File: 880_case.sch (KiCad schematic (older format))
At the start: 169 parts, among them CON1 BARREL_JACK, J1 RUN/STOP, J10 RS IN, J11 CP IN, J12 MA IN, J13 CB IN, J14 CY IN, J15 OH IN, J16 CH IN, J17 IN 1, J18 IN 2, J19 IN 3, J2 SYNC24 CLK, J20 IN 4, J21 MULT IN, J22 SUM, J23 JACK_STEREO, J24 JACK_TRS_SWITCHED, J3 ASSIGN 1, J4 ASSIGN 2, J5 BD IN, J6 SD IN, J7 LT IN, J8 MT IN, J9 HT IN, P1 CONN_02X03, P2 CONN_01X02, P3 CONN_02X08, P4 CONN_01X03, P5 CONN_01X04, P6 CONN_01X04, P7 CONN_01X03, P8 CONN_01X03, P9 CONN_01X03, Q1 MMBT3904, Q10 MMBT3904, Q11 MMBT3904, Q12 MMBT3904, Q13 MMBT3904, Q14 C945, Q15 A733, Q2 MMBT3904, Q3 MMBT3904, Q4 MMBT3904, Q5 MMBT3904, Q6 MMBT3904, Q7 MMBT3904, Q8 MMBT3904, Q9 MMBT3904, U1 74HC165, U2 74HC165, U3 VX078-500, U4 VX078-500, U5 4558, U6 4558, X1 MIDI OUT, X2 SYNC24

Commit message: more edits
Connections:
- net at J24.1 (S): now also P6.1 (P1)
- net at J24.2 (T): now also P6.2 (P2)
- net at J24.3 (TB): now also J24.5 (R), P6.3 (P3)
- net at J24.4 (RB): now also P6.4 (P4)
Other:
- note added: "R"
- note added: "RB"
- note added: "S"
- note added: "T"
- moved on the sheet: J24
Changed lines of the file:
@@
 	15200 3750 15875 3750
-$Comp
-L JACK_TRS_SWITCHED J24
-U 1 1 5C60F07A
-P 16500 1475
-F 0 "J24" H 15950 1375 60  0000 C CNN
-F 1 "JACK_TRS_SWITCHED" H 16425 1725 60  0000 C CNN
-F 2 "MyModules:RA49B14B_SWITCHCRAFT" H 16400 1475 60  0001 C CNN
-F 3 "" H 16400 1475 60  0000 C CNN
-	1    16500 1475
-	-1   0    0    -1
-$EndComp
 $Comp
 L CONN_01X03 P8
@@
 Wire Wire Line
 	21500 3875 21250 3875
-Wire Wire Line
-	16250 1325 15925 1325
-Wire Wire Line
-	16250 1425 15925 1425
-Wire Wire Line
-	15925 1600 16250 1600
 $Comp
 L R_US R67
@@
 $EndComp
 Wire Wire Line
-	15925 1500 16250 1500
-Wire Wire Line
-	15925 1500 15925 1525
-Wire Wire Line
-	15925 1600 15925 1625
-Wire Wire Line
 	15325 1625 15050 1625
 Wire Wire Line
@@
 	15050 2000 14925 2000
 Connection ~ 14925 2000
-Wire Wire Line
-	16250 1675 16100 1675
-Wire Wire Line
-	16100 1675 16100 1500
-Connection ~ 16100 1500
 $Comp
 L CONN_01X04 P5
@@
 NoConn ~ 20875 12275
 NoConn ~ 20875 12375
+Text Notes 15275 1325 0    50   ~ 0
+S
+Text Notes 15275 1525 0    50   ~ 0
+R
+$Comp
+L JACK_TRS_SWITCHED J24
+U 1 1 5C60F07A
+P 16525 1500
+F 0 "J24" H 15975 1400 60  0000 C CNN
+F 1 "JACK_TRS_SWITCHED" H 16450 1750 60  0000 C CNN
+F 2 "MyModules:RA49B14B_SWITCHCRAFT" H 16425 1500 60  0001 C CNN
+F 3 "" H 16425 1500 60  0000 C CNN
+	1    16525 1500
+	-1   0    0    1
+$EndComp
+Wire Wire Line
+	15925 1325 16150 1325
+Text Notes 15275 1625 0    50   ~ 0
+RB
+Text Notes 15275 1425 0    50   ~ 0
+T
+Wire Wire Line
+	16150 1425 16050 1425
+Wire Wire Line
+	16050 1425 16050 1675
+Wire Wire Line
+	16050 1675 16150 1675
+Wire Wire Line
+	15925 1525 16050 1525
+Connection ~ 16050 1525
+Wire Wire Line
+	16150 1500 16125 1500
+Wire Wire Line
+	16125 1500 16125 1450
+Wire Wire Line
+	16125 1450 15925 1450
+Wire Wire Line
+	15925 1450 15925 1425
+Wire Wire Line
+	16150 1600 15925 1600
+Wire Wire Line
+	15925 1600 15925 1625
 $EndSCHEMATC

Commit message: added power switch and balanced jack sub boards
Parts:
- added J25: JACK_STEREO, MyModules:11XPC-SWITCH_CRAFT, symbol JACK_STEREO
- added P10: CONN_01X02, Pin_Headers:Pin_Header_Straight_1x02_Pitch2.54mm, symbol CONN_01X02
- added P11: CONN_01X03, Pin_Headers:Pin_Header_Straight_1x03_Pitch2.54mm, symbol CONN_01X03
- added SW1: SPST, MyModules:PR_PPR_ROCKER_SW, symbol SPST
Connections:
- new net: P10.1 (P1), SW1.2
- new net: P10.2 (P2), SW1.1
- new net: J25.1, P11.1 (P1)
- new net: J25.2, P11.2 (P2)
- new net: J25.3, P11.3 (P3)
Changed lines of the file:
@@
 Wire Wire Line
 	12125 4125 12125 4300
-Text Notes 19225 2475 0    100  ~ 0
+Text Notes 19125 2075 0    100  ~ 0
 TO TRS OUT
 $Comp
@@
 Wire Wire Line
 	15925 1600 15925 1625
+$Comp
+L CONN_01X02 P10
+U 1 1 5CF5764A
+P 14875 11125
+F 0 "P10" H 14875 11275 50  0000 C CNN
+F 1 "CONN_01X02" V 14975 11125 50  0000 C CNN
+F 2 "Pin_Headers:Pin_Header_Straight_1x02_Pitch2.54mm" H 14875 11125 60  0001 C CNN
+F 3 "" H 14875 11125 60  0000 C CNN
+	1    14875 11125
+	0    1    1    0
+$EndComp
+$Comp
+L SPST SW1
+U 1 1 5CF577D2
+P 14825 10375
+F 0 "SW1" H 14825 10475 50  0000 C CNN
+F 1 "SPST" H 14825 10275 50  0000 C CNN
+F 2 "MyModules:PR_PPR_ROCKER_SW" H 14825 10375 60  0000 C CNN
+F 3 "" H 14825 10375 60  0000 C CNN
+	1    14825 10375
+	1    0    0    -1
+$EndComp
+Wire Wire Line
+	14325 10375 14325 10925
+Wire Wire Line
+	15325 10375 15325 10925
+Wire Wire Line
+	14325 10925 14825 10925
+Wire Wire Line
+	15325 10925 14925 10925
+$Comp
+L JACK_STEREO J25
+U 1 1 5CF60EBD
+P 19950 2475
+F 0 "J25" H 19400 2375 60  0000 C CNN
+F 1 "JACK_STEREO" H 19700 2675 60  0000 C CNN
+F 2 "MyModules:11XPC-SWITCH_CRAFT" H 19850 2475 60  0001 C CNN
+F 3 "" H 19850 2475 60  0000 C CNN
+	1    19950 2475
+	-1   0    0    -1
+$EndComp
+$Comp
+L CONN_01X03 P11
+U 1 1 5CF61677
+P 19350 2425
+F 0 "P11" H 19350 2625 50  0000 C CNN
+F 1 "CONN_01X03" V 19450 2425 50  0000 C CNN
+F 2 "Pin_Headers:Pin_Header_Straight_1x03_Pitch2.54mm" H 19350 2425 60  0001 C CNN
+F 3 "" H 19350 2425 60  0000 C CNN
+	1    19350 2425
+	-1   0    0    -1
+$EndComp
+Text Notes 19500 2325 0    60   ~ 0
+S
+Text Notes 19500 2425 0    60   ~ 0
+T
+Text Notes 19500 2525 0    60   ~ 0
+R
+Wire Wire Line
+	19700 2325 19550 2325
+Wire Wire Line
+	19550 2425 19650 2425
+Wire Wire Line
+	19650 2425 19650 2625
+Wire Wire Line
+	19650 2625 19700 2625
+Wire Wire Line
+	19700 2425 19700 2525
+Wire Wire Line
+	19700 2525 19550 2525
 $EndSCHEMATC

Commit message: panelizing pcb
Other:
- note added: "DELETE C15, R53?"
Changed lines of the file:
@@
 Wire Wire Line
 	19700 2525 19550 2525
+Text Notes 13100 2325 0    100  ~ 0
+DELETE C15, R53?
 $EndSCHEMATC

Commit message: commit before checkout of new branch
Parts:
- D17: value D_Schottky -> MBRS240LT3G
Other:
- note added: "50 V"
- note added: "C12 and C16 - too much rolloff?\nChange to 100p? 22p? 10p?"
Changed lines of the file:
@@
 P 15400 11825
 F 0 "D17" H 15400 11925 50  0000 C CNN
-F 1 "D_Schottky" H 15400 11725 50  0000 C CNN
+F 1 "MBRS240LT3G" H 15400 11725 50  0000 C CNN
 F 2 "MyModules:SMB-1C2A" H 15400 11825 60  0001 C CNN
 F 3 "" H 15400 11825 60  0000 C CNN
@@
 Text Notes 13100 2325 0    100  ~ 0
 DELETE C15, R53?
+Text Notes 15825 12450 0    50   ~ 0
+50 V
+Text Notes 11475 2100 0    100  ~ 0
+C12 and C16 - too much rolloff?\nChange to 100p? 22p? 10p?
 $EndSCHEMATC

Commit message: separating digital and audio gnd planes
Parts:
- removed C15: 33μ, Capacitors_SMD:CP_Elec_5x5.3, symbol CP_US
- removed P9: CONN_01X03, Pin_Headers:Pin_Header_Straight_1x03_Pitch2.54mm, symbol CONN_01X03
- removed Q13: MMBT3904, MyModules:SOT23-132-JRL, symbol C945
- removed R44: 100K, MyModules:SM0603-R-YAGEO, symbol R_US
- removed R45: 10K, MyModules:SM0603-R-YAGEO, symbol R_US
- removed R53: 330K, MyModules:SM0603-R-YAGEO, symbol R_US
- added C15: 1µ, Capacitors_SMD:C_0805, symbol C_US
- added C19: 0.1µ, MyModules:SM0603-C-MURATA, symbol C_US
- R42: value 10K -> 47K
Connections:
- net ~CE is gone; now on net GNDD: U1.15 (~CE), U2.15 (~CE)
- net +5V: now also C15.1, C19.1; no longer R42.1
- net DIN_FILL: now also R43.1
- net DIN_RESET: now also R42.1
- net GND: no longer C1.2, C2.2, C3.2, D10.2 (A), D11.2 (A), D12.2 (A), D13.2 (A), D14.2 (A), D15.2 (A), D16.2 (A), D2.2 (A), D4.2 (A), D5.2 (A), D6.2 (A), D7.2 (A), D8.2 (A), D9.2 (A), ISP1.6 (P6), J1.1, J10.1, J10.2, J11.1, J11.2, J12.1, J12.2, J13.1, J13.2, J14.1, J14.2, J15.1, J15.2, J16.1, J16.2, J2.1, J3.1, J4.1, J5.1, J5.2, J6.1, J6.2, J7.1, J7.2, J8.1, J8.2, J9.1, J9.2, P1.3 (P3), P7.3 (P3), Q1.2 (E), Q10.2 (E), Q11.2 (E), Q12.2 (E), Q2.2 (E), Q3.2 (E), Q4.2 (E), Q5.2 (E), Q6.2 (E), Q7.2 (E), Q8.2 (E), Q9.2 (E), R10.2, R11.2, R12.2, R13.2, R2.1, R22.2, R23.2, R24.2, R25.2, R34.2, R35.2, R36.2, R37.2, U1.8 (GND), U2.3 (D4), U2.4 (D5), U2.5 (D6), U2.6 (D7), U2.8 (GND), X1.2
- net GNDD: now reaches R43.2
- net GNDD: now also C1.2, C2.2, C3.2, D10.2 (A), D11.2 (A), D12.2 (A), D13.2 (A), D14.2 (A), D15.2 (A), D16.2 (A), D2.2 (A), D4.2 (A), D5.2 (A), D6.2 (A), D7.2 (A), D8.2 (A), D9.2 (A), ISP1.6 (P6), J1.1, J10.1, J10.2, J11.1, J11.2, J12.1, J12.2, J13.1, J13.2, J14.1, J14.2, J15.1, J15.2, J16.1, J16.2, J2.1, J3.1, J4.1, J5.1, J5.2, J6.1, J6.2, J7.1, J7.2, J8.1, J8.2, J9.1, J9.2, P1.3 (P3), Q1.2 (E), Q10.2 (E), Q11.2 (E), Q12.2 (E), Q2.2 (E), Q3.2 (E), Q4.2 (E), Q5.2 (E), Q6.2 (E), Q7.2 (E), Q8.2 (E), Q9.2 (E), R10.2, R11.2, R12.2, R13.2, R2.1, R22.2, R23.2, R24.2, R25.2, R34.2, R35.2, R36.2, R37.2, R42.2, U1.8 (GND), U2.3 (D4), U2.4 (D5), U2.5 (D6), U2.6 (D7), U2.8 (GND), X1.2, C15.2, C19.2
- removed net ~RESET: ISP1.5 (P5), R42.2, R43.1
- new net PHONE_GND: P7.3 (P3)
- no-connect marks 20 -> 21
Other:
- note added: "MISO IS TRIGGER_2\nANYWAY TO ISOLATE THROUGH A BUFFER?"
- note removed: "Is pull-up here\nreally necessary?\nMay cause trouble with \nreset, delete or increase?"
- note removed: "Probably want to tri-state\n74HC165s during ISP programming.\nJumper makes this optional"
- moved on the sheet: R42, R43

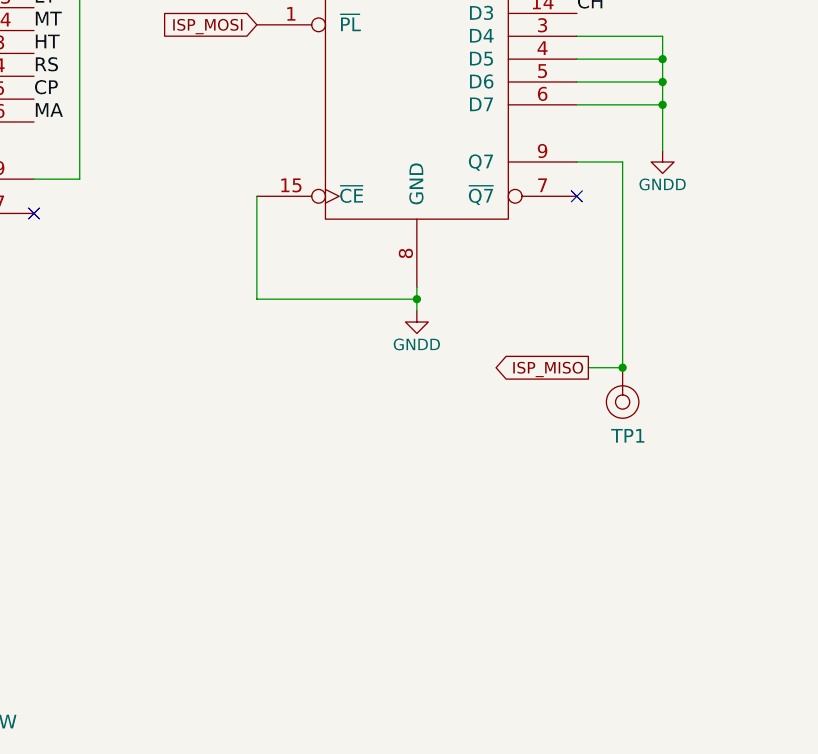
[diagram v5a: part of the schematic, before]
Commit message: working on 4 layer, separate digital and audio gnd planes
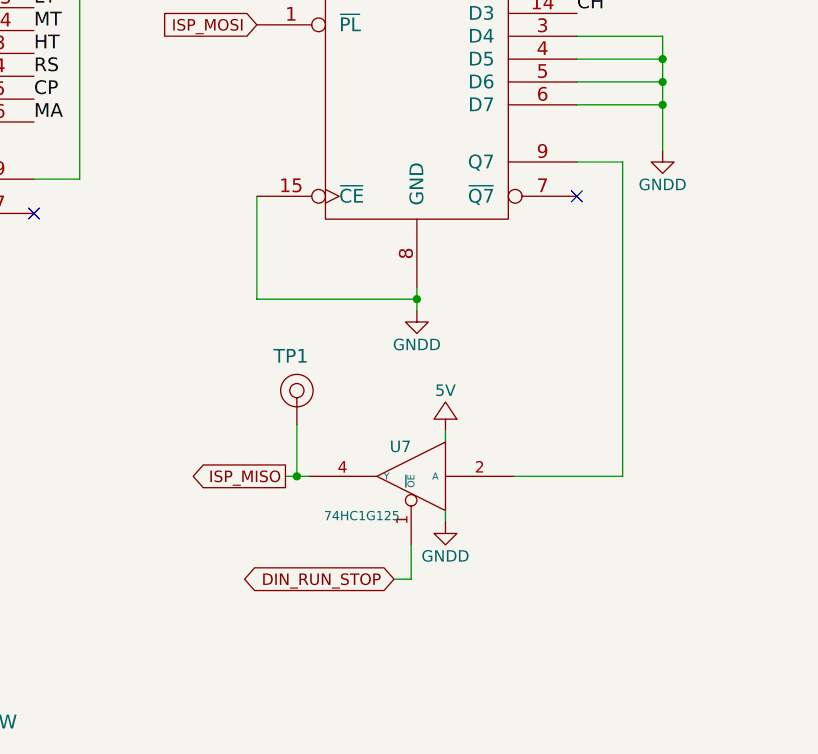
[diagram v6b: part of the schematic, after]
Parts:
- added U7: 74HC1G125, Housings_SSOP:TSOP-5_1.65x3.05mm_Pitch0.95mm, symbol 74HC1G125
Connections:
- net +5V: now also U7.6 (VCC)
- net DIN_RUN_STOP: now also U7.1 (~OE)
- net GNDD: now also U7.3 (GNDD)
- net ISP_MISO: now also U7.4 (Y); no longer U2.9 (Q7)
- new net: U2.9 (Q7), U7.2 (A)
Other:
- moved on the sheet: TP1
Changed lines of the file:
@@
 L CONN_1 TP1
 U 1 1 5C4B2D94
-P 18150 8975
-F 0 "TP1" V 18300 8925 60  0000 L CNN
-F 1 "CONN_1" H 18150 9030 30  0001 C CNN
-F 2 "MyModules:TEST_POINT_LOOP_4592" H 18150 8975 60  0001 C CNN
-F 3 "" H 18150 8975 60  0000 C CNN
-	1    18150 8975
-	0    1    1    0
+P 16725 8925
+F 0 "TP1" V 16875 8875 60  0000 L CNN
+F 1 "CONN_1" H 16725 8980 30  0001 C CNN
+F 2 "MyModules:TEST_POINT_LOOP_4592" H 16725 8925 60  0001 C CNN
+F 3 "" H 16725 8925 60  0000 C CNN
+	1    16725 8925
+	0    -1   -1   0
 $EndComp
 $Comp
@@
 	18150 7925 17950 7925
 Wire Wire Line
-	18150 7925 18150 8825
-Wire Wire Line
-	18150 8825 18000 8825
-Connection ~ 18150 8825
+	18150 9300 18150 7925
 Connection ~ 17250 6075
 Wire Wire Line
@@
 Text GLabel 16550 7125 0    50   BiDi ~ 0
 ISP_SCK
-Text GLabel 18000 8825 0    50   Output ~ 0
+Text GLabel 16675 9300 0    50   Output ~ 0
 ISP_MISO
 Text GLabel 14175 7400 0    50   Input ~ 0
@@
 Wire Wire Line
 	1900 4425 1900 4550
-Wire Wire Line
-	1900 3700 1900 3825
 Text GLabel 1900 3400 0    60   BiDi ~ 0
 DIN_RUN_STOP
-NoConn ~ 1900 3550
 NoConn ~ 1900 4275
 $Comp
@@
 	16550 8525 17250 8525
 Connection ~ 17250 8525
+$Comp
+L 74HC1G125 U7
+U 1 1 5D8C7D38
+P 17225 9300
+F 0 "U7" H 17225 9400 50  0000 L BNN
+F 1 "74HC1G125" H 17275 9150 40  0000 L TNN
+F 2 "Housings_SSOP:TSOP-5_1.65x3.05mm_Pitch0.95mm" H 17225 9300 60  0001 C CNN
+F 3 "" H 17225 9300 60  0000 C CNN
+	1    17225 9300
+	-1   0    0    -1
+$EndComp
+Wire Wire Line
+	17675 9300 18150 9300
+$Comp
+L GNDD #PWR095
+U 1 1 5D8C997F
+P 17375 9500
+F 0 "#PWR095" H 17375 9250 50  0001 C CNN
+F 1 "GNDD" H 17375 9350 50  0000 C CNN
+F 2 "" H 17375 9500 60  0000 C CNN
+F 3 "" H 17375 9500 60  0000 C CNN
+	1    17375 9500
+	1    0    0    -1
+$EndComp
+$Comp
+L 5V #PWR096
+U 1 1 5D8CAB02
+P 17375 9100
+F 0 "#PWR096" H 17375 8950 50  0001 C CNN
+F 1 "5V" H 17375 9275 50  0000 C CNN
+F 2 "" H 17375 9100 60  0000 C CNN
+F 3 "" H 17375 9100 60  0000 C CNN
+	1    17375 9100
+	1    0    0    -1
+$EndComp
+Text GLabel 17150 9750 0    50   BiDi ~ 0
+DIN_RUN_STOP
+Wire Wire Line
+	17225 9600 17225 9750
+Wire Wire Line
+	17225 9750 17150 9750
+Wire Wire Line
+	1900 3700 1900 3825
+NoConn ~ 1900 3550
+Wire Wire Line
+	16675 9300 16775 9300
+Wire Wire Line
+	16725 9075 16725 9300
+Connection ~ 16725 9300
+Wire Wire Line
+	17375 9100 17375 9150
+Wire Wire Line
+	17375 9500 17375 9450
 $EndSCHEMATC

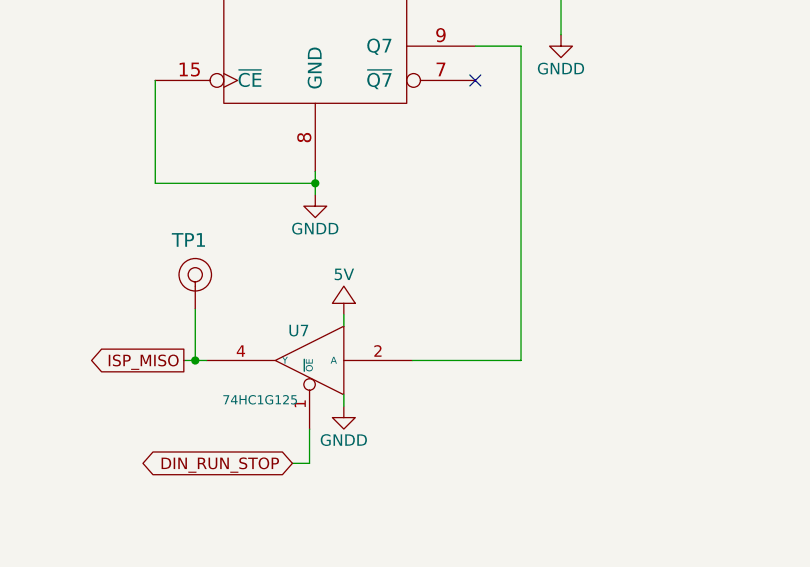
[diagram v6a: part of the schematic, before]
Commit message: 4 layer, added tri-state buffer on MISO line, ordered prototype PCB
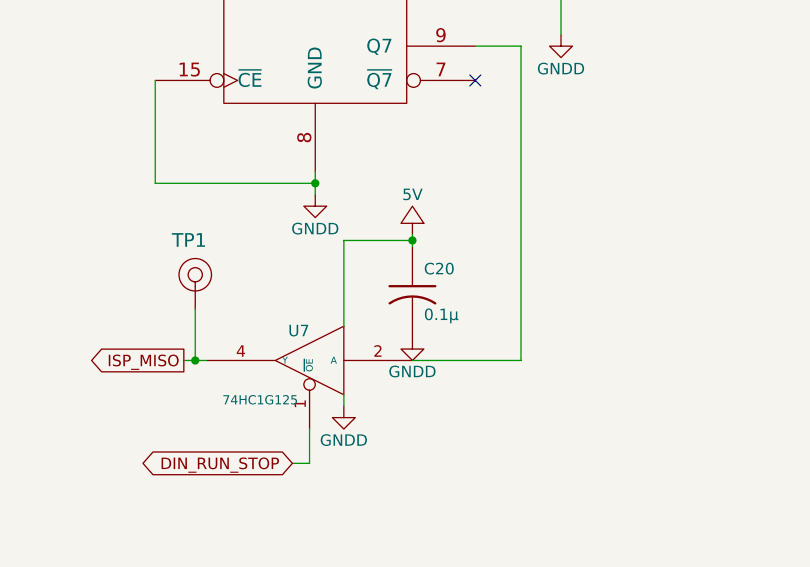
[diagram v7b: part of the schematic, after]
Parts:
- added C20: 0.1µ, MyModules:SM0603-C-MURATA, symbol C_US
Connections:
- net +5V: now also C20.1
- net GNDD: now also C20.2

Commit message: few tweaks before panelizing. kept 74HCT1G125GV footprint as TSOP-5-SC74A-SOT-753, which is the larger of the two available footprints for U7
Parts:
- added R44, R45: 47K, MyModules:SM0603-R-YAGEO, symbol R_US
- U7: value 74HC1G125 -> 74HCT1G125GV
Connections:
- net PHONE_GND is gone; now on net GND: P7.3 (P3)
- net +5V: now also R44.1
- net GNDD: now also R45.2
- net ISP_MISO: now also R44.2, R45.1
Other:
- note added: "PULL UP HERE"
- note added: "PULL UP OR DOWN HERE?"
- note added: "TRS SWITCHED PIN OUT WRONG - FIX! (ED?)"
- note added: "TSOP-5-SC74A-SOT-753"
- note removed: "DELETE C15, R53?"
- note removed: "MISO IS TRIGGER_2\nANYWAY TO ISOLATE THROUGH A BUFFER?"
- note removed: "TRS SWITCHED PIN OUT WRONG - FIX!"
